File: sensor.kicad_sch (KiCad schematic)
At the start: 3 parts, among them U5 MS5837-xxBA

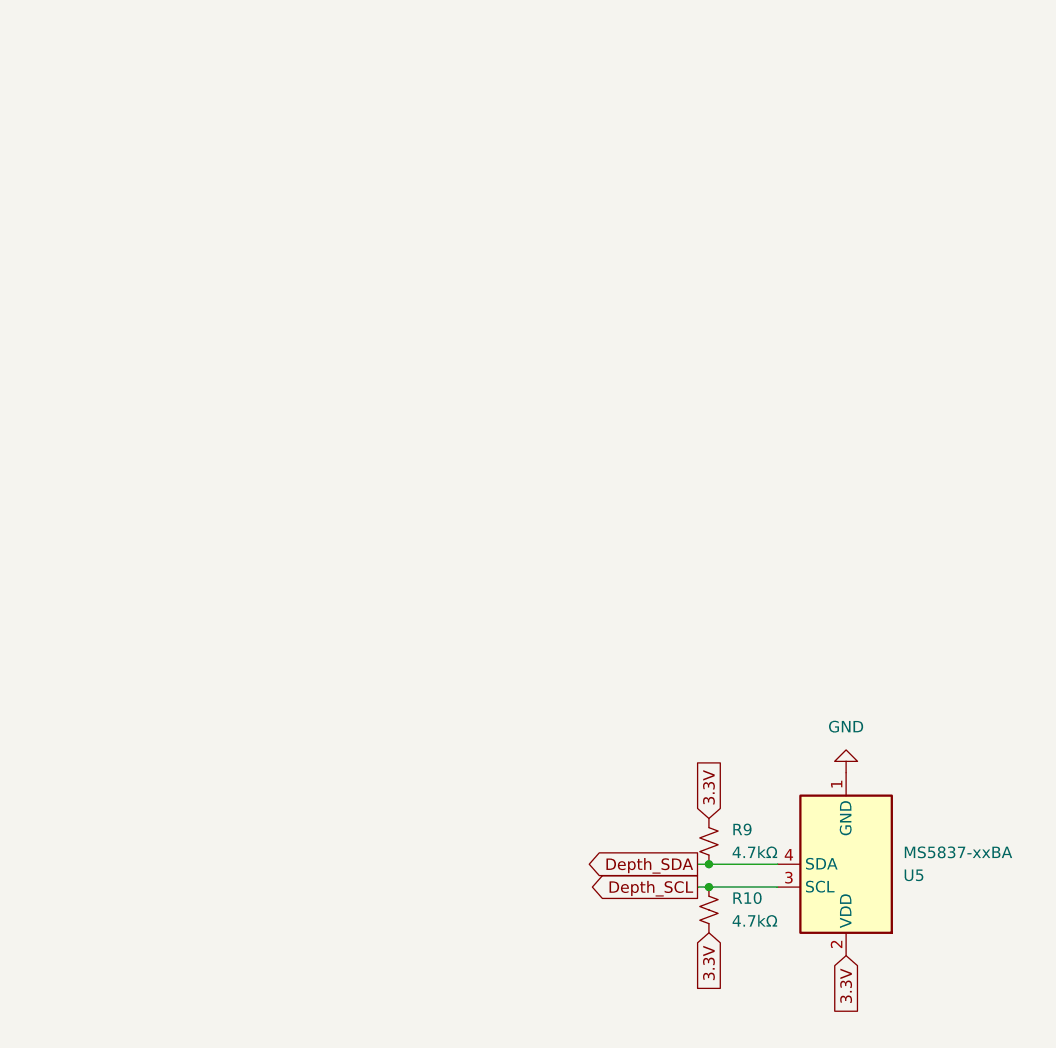
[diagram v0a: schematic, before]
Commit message: Overhaul
Overhauled the schematic so all the components are correct, rewired power to be 12 V instead of 9 V and connected hierarchical labels between modules. Added more decoupling capacitors where they were missing.
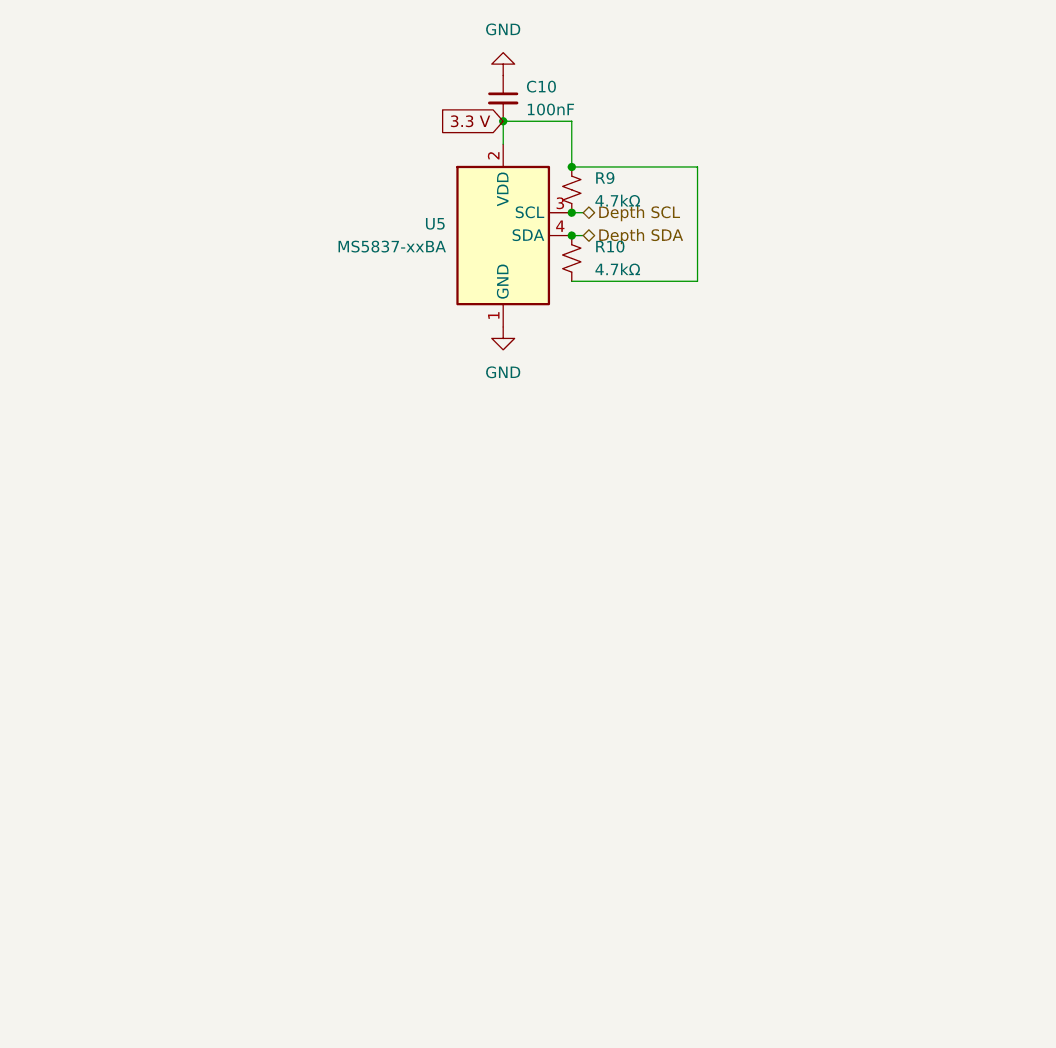
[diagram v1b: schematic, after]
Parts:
- added C10: 100nF, symbol Device:C_Small
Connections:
- net GND: now also C10.1
- net 3.3V renamed 3.3 V
- net 3.3 V: now also C10.2
- net Depth_SCL renamed Depth SCL
- net Depth SCL: now also R9.2; no longer R10.1
- net Depth_SDA renamed Depth SDA
- net Depth SDA: now also R10.1; no longer R9.2

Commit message: started layout
in meeting
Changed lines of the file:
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@@
+	(wire
+		(pts
+			(xy 39.37 27.94) (xy 40.64 27.94)
+		)
+		(stroke
+			(width 0)
+			(type default)
+		)
+	)
 	(wire
 		(pts
@@
 	(global_label "3.3 V"
 		(shape input)
-		(at 40.64 27.94 180)
+		(at 39.37 27.94 180)
 		(fields_autoplaced yes)
 		(effects
@@
 		)
 		(property "Intersheetrefs" "${INTERSHEET_REFS}"
-			(at 32.5748 27.94 0)
+			(at 31.3048 27.94 0)
 			(hide yes)
 			(show_name no)

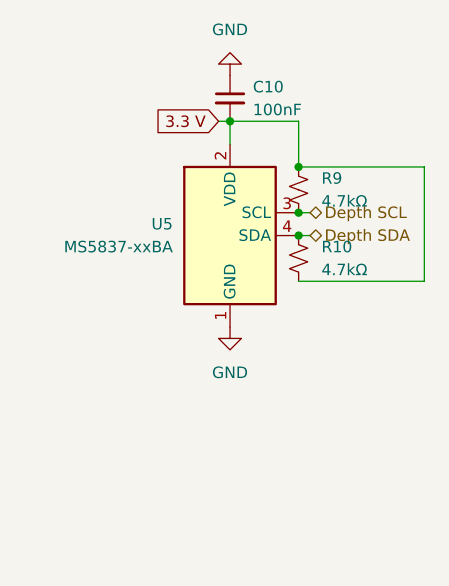
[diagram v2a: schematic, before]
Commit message: Footprint
Found footprints for multiple components and imported them to be used in PCB
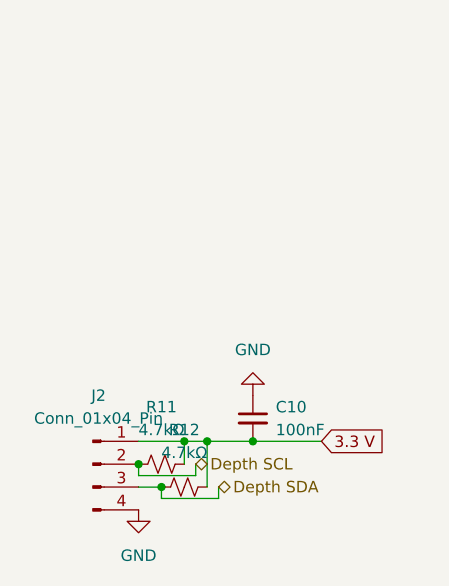
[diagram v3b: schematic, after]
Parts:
- removed R10, R9: 4.7kΩ, symbol Device:R_Small_US
- removed U5: MS5837-xxBA, Sensor_Pressure:TE_MS5837-xxBA, symbol Sensor_Pressure:MS5837-xxBA
- added J2: Conn_01x04_Pin, symbol Connector:Conn_01x04_Pin
- added R11, R12: 4.7kΩ, symbol Device:R_Small_US
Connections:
- net 3.3 V: now also J2.1 (Pin_1), R11.2, R12.2
- net Depth SCL: now also J2.2 (Pin_2), R11.1
- net Depth SDA: now also J2.3 (Pin_3), R12.1
- net GND: now also J2.4 (Pin_4)
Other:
- moved on the sheet: C10

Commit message: Gave footprints to everything
Footprints
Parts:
- C10: footprint (none) -> Capacitor_SMD:C_0603_1608Metric
- J2: footprint (none) -> Connector_JST:JST_GH_BM04B-GHS-TBT_1x04-1MP_P1.25mm_Vertical
- R11, R12: footprint (none) -> Resistor_SMD:R_0603_1608Metric
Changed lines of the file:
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@@
 			)
 		)
-		(property "Footprint" ""
+		(property "Footprint" "Resistor_SMD:R_0603_1608Metric"
 			(at 35.56 68.58 0)
 			(hide yes)
@@
 			)
 		)
-		(property "Footprint" ""
+		(property "Footprint" "Connector_JST:JST_GH_BM04B-GHS-TBT_1x04-1MP_P1.25mm_Vertical"
 			(at 25.4 66.04 0)
 			(hide yes)
@@
 			)
 		)
-		(property "Footprint" ""
+		(property "Footprint" "Capacitor_SMD:C_0603_1608Metric"
 			(at 43.18 60.96 0)
 			(hide yes)
@@
 			)
 		)
-		(property "Footprint" ""
+		(property "Footprint" "Resistor_SMD:R_0603_1608Metric"
 			(at 33.02 66.04 0)
 			(hide yes)

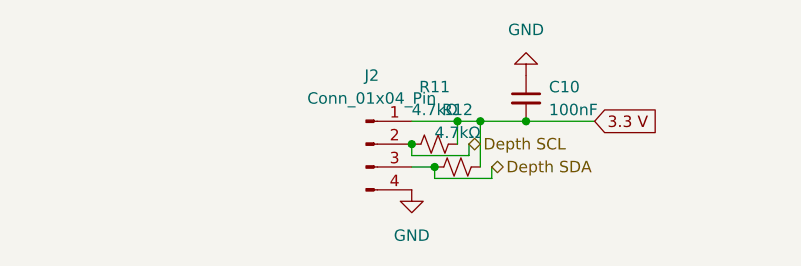
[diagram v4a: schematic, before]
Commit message: USB-C + Complete wiring
Compltetly wired the pcb (I don't understand the DRC errors) and added a usb C to flash the stm, modified the switch to be the BOOT0 for the stm so it controls whether the stm is in flash mode
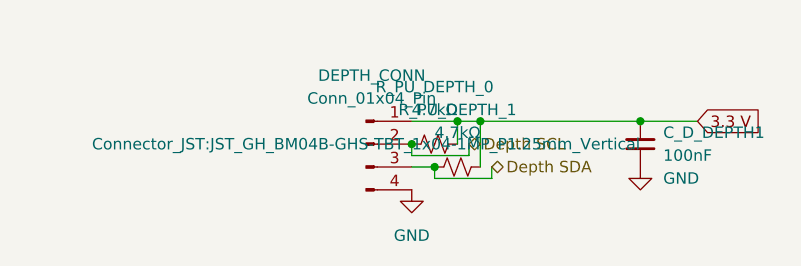
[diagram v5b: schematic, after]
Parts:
- renumbered C10 to C_D_DEPTH1, J2 to DEPTH_CONN, R11 to R_PU_DEPTH_0, R12 to R_PU_DEPTH_1
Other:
- moved on the sheet: C_D_DEPTH1
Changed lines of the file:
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@@
-	)
-	(junction
-		(at 43.18 63.5)
-		(diameter 0)
-		(color 0 0 0 0)
 	)
 	(junction
@@
 		(color 0 0 0 0)
 	)
+	(junction
+		(at 55.88 63.5)
+		(diameter 0)
+		(color 0 0 0 0)
+	)
 	(wire
 		(pts
@@
 	(wire
 		(pts
-			(xy 38.1 63.5) (xy 43.18 63.5)
-		)
-		(stroke
-			(width 0)
-			(type default)
-		)
-	)
-	(wire
-		(pts
 			(xy 36.83 66.04) (xy 36.83 67.31)
 		)
@@
 	(wire
 		(pts
+			(xy 55.88 63.5) (xy 62.23 63.5)
+		)
+		(stroke
+			(width 0)
+			(type default)
+		)
+	)
+	(wire
+		(pts
 			(xy 30.48 63.5) (xy 35.56 63.5)
 		)
@@
 	(wire
 		(pts
-			(xy 43.18 63.5) (xy 50.8 63.5)
-		)
-		(stroke
-			(width 0)
-			(type default)
-		)
-	)
-	(wire
-		(pts
 			(xy 35.56 63.5) (xy 38.1 63.5)
 		)
@@
 		(pts
 			(xy 33.02 68.58) (xy 30.48 68.58)
+		)
+		(stroke
+			(width 0)
+			(type default)
+		)
+	)
+	(wire
+		(pts
+			(xy 38.1 63.5) (xy 55.88 63.5)
 		)
 		(stroke
@@
 	(global_label "3.3 V"
 		(shape input)
-		(at 50.8 63.5 0)
+		(at 62.23 63.5 0)
 		(fields_autoplaced yes)
 		(effects
@@
 		)
 		(property "Intersheetrefs" "${INTERSHEET_REFS}"
-			(at 58.8652 63.5 0)
+			(at 70.2952 63.5 0)
 			(hide yes)
 			(show_name no)
@@
 		(dnp no)
 		(fields_autoplaced yes)
-		(property "Reference" "R12"
+		(property "Reference" "R_PU_DEPTH_1"
 			(at 35.56 62.23 90)
 			(show_name no)
@@
 			(project "X19-Float-Board"
 				(path "/00000000-0000-0000-0000-000060e6118b/5f356ab3-657b-42f3-9a8b-ebc79580ebf5"
-					(reference "R12")
+					(reference "R_PU_DEPTH_1")
 					(unit 1)
 				)
@@
 		(dnp no)
 		(fields_autoplaced yes)
-		(property "Reference" "J2"
+		(property "Reference" "DEPTH_CONN"
 			(at 26.035 58.42 0)
 			(show_name no)
@@
 		(property "Footprint" "Connector_JST:JST_GH_BM04B-GHS-TBT_1x04-1MP_P1.25mm_Vertical"
 			(at 25.4 66.04 0)
-			(hide yes)
 			(show_name no)
 			(do_not_autoplace no)
@@
 			(project "X19-Float-Board"
 				(path "/00000000-0000-0000-0000-000060e6118b/5f356ab3-657b-42f3-9a8b-ebc79580ebf5"
-					(reference "J2")
+					(reference "DEPTH_CONN")
 					(unit 1)
 				)
@@
 	(symbol
 		(lib_id "Device:C_Small")
-		(at 43.18 60.96 0)
+		(at 55.88 66.04 180)
 		(unit 1)
 		(body_style 1)
@@
 		(dnp no)
 		(fields_autoplaced yes)
-		(property "Reference" "C10"
-			(at 45.72 59.6962 0)
-			(show_name no)
-			(do_not_autoplace no)
-			(effects
-				(font
-					(size 1.27 1.27)
-				)
-				(justify left)
+		(property "Reference" "C_D_DEPTH1"
+			(at 58.42 64.7635 0)
+			(show_name no)
+			(do_not_autoplace no)
+			(effects
+				(font
+					(size 1.27 1.27)
+				)
+				(justify right)
 			)
 		)
 		(property "Value" "100nF"
-			(at 45.72 62.2362 0)
-			(show_name no)
-			(do_not_autoplace no)
-			(effects
-				(font
-					(size 1.27 1.27)
-				)
-				(justify left)
+			(at 58.42 67.3035 0)
+			(show_name no)
+			(do_not_autoplace no)
+			(effects
+				(font
+					(size 1.27 1.27)
+				)
+				(justify right)
 			)
 		)
 		(property "Footprint" "Capacitor_SMD:C_0603_1608Metric"
-			(at 43.18 60.96 0)
+			(at 55.88 66.04 0)
 			(hide yes)
 			(show_name no)
@@
 		)
 		(property "Datasheet" ""
-			(at 43.18 60.96 0)
+			(at 55.88 66.04 0)
 			(hide yes)
 			(show_name no)
@@
 		)
 		(property "Description" "Unpolarized capacitor, small symbol"
-			(at 43.18 60.96 0)
+			(at 55.88 66.04 0)
 			(hide yes)
 			(show_name no)
@@
 			(project "X19-Float-Board"
 				(path "/00000000-0000-0000-0000-000060e6118b/5f356ab3-657b-42f3-9a8b-ebc79580ebf5"
-					(reference "C10")
+					(reference "C_D_DEPTH1")
 					(unit 1)
 				)
@@
 	(symbol
 		(lib_id "power:GND")
-		(at 43.18 58.42 180)
+		(at 55.88 68.58 0)
 		(unit 1)
 		(body_style 1)
@@
 		(fields_autoplaced yes)
 		(property "Reference" "#PWR015"
-			(at 43.18 52.07 0)
+			(at 55.88 74.93 0)
 			(hide yes)
 			(show_name no)
@@
 		)
 		(property "Value" "GND"
-			(at 43.18 53.34 0)
-			(show_name no)
-			(do_not_autoplace no)
-			(effects
-				(font
-					(size 1.27 1.27)
-				)
+			(at 58.42 69.8499 0)
+			(show_name no)
+			(do_not_autoplace no)
+			(effects
+				(font
+					(size 1.27 1.27)
+				)
+				(justify left)
 			)
 		)
 		(property "Footprint" ""
-			(at 43.18 58.42 0)
+			(at 55.88 68.58 0)
 			(hide yes)
 			(show_name no)
@@
 		)
 		(property "Datasheet" ""
-			(at 43.18 58.42 0)
+			(at 55.88 68.58 0)
 			(hide yes)
 			(show_name no)
@@
 		)
 		(property "Description" "Power symbol creates a global label with name \"GND\" , ground"
-			(at 43.18 58.42 0)
+			(at 55.88 68.58 0)
 			(hide yes)
 			(show_name no)
@@
 		(dnp no)
 		(fields_autoplaced yes)
-		(property "Reference" "R11"
+		(property "Reference" "R_PU_DEPTH_0"
 			(at 33.02 59.69 90)
 			(show_name no)
@@
 			(project "X19-Float-Board"
 				(path "/00000000-0000-0000-0000-000060e6118b/5f356ab3-657b-42f3-9a8b-ebc79580ebf5"
-					(reference "R11")
+					(reference "R_PU_DEPTH_0")
 					(unit 1)
 				)

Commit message: Checkpoint
Checkpoint, pre battery telemetry, pre new stm
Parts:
- renumbered DEPTH_CONN to DEPTH_CONN1
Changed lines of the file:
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@@
 		(dnp no)
 		(fields_autoplaced yes)
-		(property "Reference" "DEPTH_CONN"
+		(property "Reference" "DEPTH_CONN1"
 			(at 26.035 58.42 0)
 			(show_name no)
@@
 			(project "X19-Float-Board"
 				(path "/00000000-0000-0000-0000-000060e6118b/5f356ab3-657b-42f3-9a8b-ebc79580ebf5"
-					(reference "DEPTH_CONN")
+					(reference "DEPTH_CONN1")
 					(unit 1)
 				)

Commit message: Update
Update
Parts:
- added R12: 10k, symbol Device:R_Small_US
- added R13: Generic Photoresistor, symbol Device:R_Photo
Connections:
- net 3.3 V: now also R13.1
- net GND: now also R12.1
- new net LIGHT VOLTAGE: R12.2, R13.2

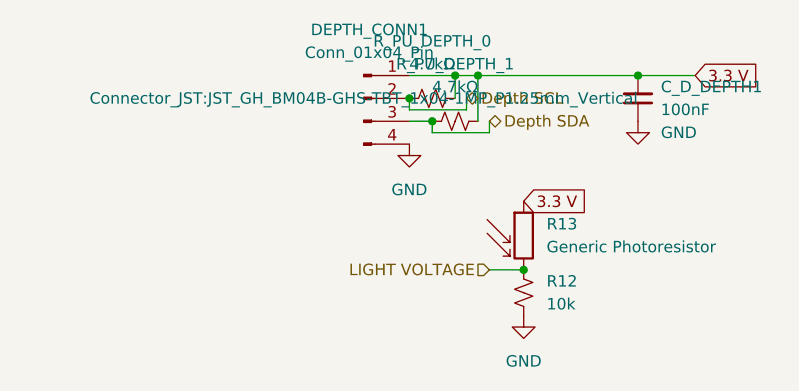
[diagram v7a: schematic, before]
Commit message: todolist update
update of the to do list on schematic
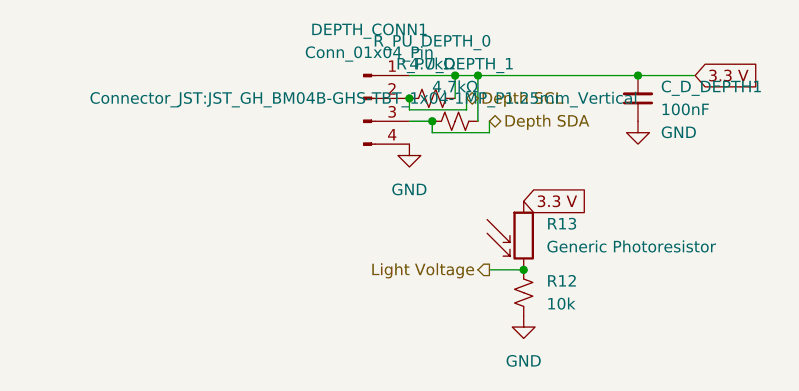
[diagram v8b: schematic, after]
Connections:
- net LIGHT VOLTAGE renamed Light Voltage
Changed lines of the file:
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@@
 		)
 	)
-	(hierarchical_label "LIGHT VOLTAGE"
-		(shape input)
+	(hierarchical_label "Light Voltage"
+		(shape output)
 		(at 39.37 85.09 180)
 		(effects
